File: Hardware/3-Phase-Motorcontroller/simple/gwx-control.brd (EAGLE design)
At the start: 54 x 36 mm, 25 parts, among them IC1 74LS02D, IC2 74LS123D, T1 BC850, T2 BC850

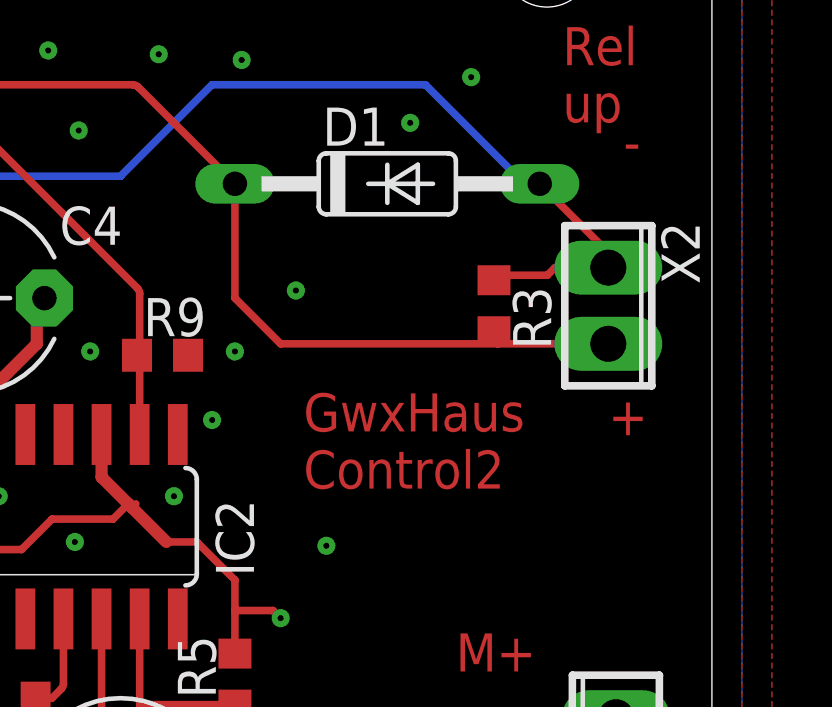
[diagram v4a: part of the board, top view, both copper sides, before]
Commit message: added alternative SMD diode
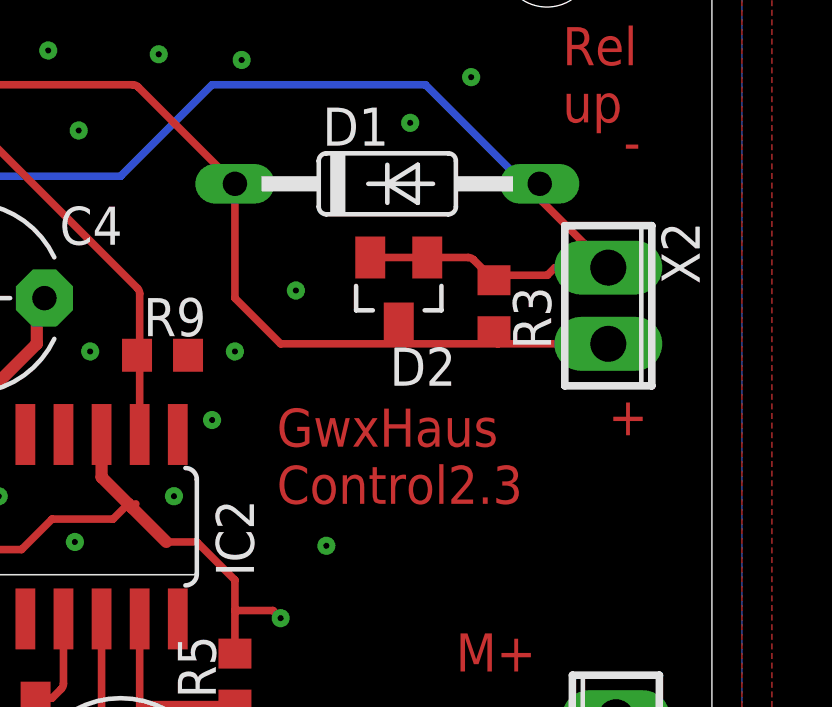
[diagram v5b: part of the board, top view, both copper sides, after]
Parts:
- added D2: BAT54C, diode:SOT23
- D1: value 1N4148DO35-10 -> 1N4148
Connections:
- net /UP: now also D2.1, D2.2
- net VCC: now also D2.3
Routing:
- net /UP: track 67.9 -> 72.3 mm
- net VCC: track 139.8 -> 140.5 mm
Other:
- board text added: "GwxHaus Control2.3"
- board text removed: "GwxHaus Control2"
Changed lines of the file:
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@@
 <text x="0.46" y="19.558" size="1.778" layer="1">eu</text>
 <text x="0.46" y="17.018" size="1.778" layer="1">ed</text>
-<text x="40.386" y="15.748" size="1.27" layer="1">GwxHaus
-Control2</text>
+<text x="39.497" y="15.24" size="1.27" layer="1">GwxHaus
+Control2.3</text>
 <text x="45.466" y="9.652" size="1.27" layer="1">M+</text>
 <text x="49.022" y="27.956" size="1.27" layer="1">Rel
@@
 </autorouter>
 <elements>
-<element name="D1" library="diode" package="DO35-10" value="1N4148DO35-10" x="43.18" y="25.908"/>
+<element name="D1" library="diode" package="DO35-10" value="1N4148" x="43.18" y="25.908"/>
 <element name="IC1" library="74xx-eu" package="SO14" value="74LS02D" x="16.51" y="14.478" smashed="yes">
 <attribute name="VALUE" x="13.335" y="13.716" size="1.27" layer="27" ratio="10"/>
@@
 <element name="T2" library="transistor" package="SOT23-BEC" value="BC850" x="27.178" y="4.953" rot="R270"/>
 <element name="R10" library="resistor" package="R0603" value="10k" x="30.607" y="8.763" rot="R180"/>
+<element name="D2" library="diode" package="SOT23" value="BAT54C" x="43.561" y="22.352" rot="R180"/>
 </elements>
 <signals>
@@
 <via x="21.844" y="21.844" extent="1-16" drill="0.2" diameter="0.254"/>
 <wire x1="38.1" y1="22.098" x2="39.624" y2="20.574" width="0.254" layer="1"/>
-<wire x1="39.624" y1="20.574" x2="46.863" y2="20.574" width="0.254" layer="1"/>
+<wire x1="39.624" y1="20.574" x2="43.688" y2="20.574" width="0.254" layer="1"/>
+<wire x1="43.688" y1="20.574" x2="46.863" y2="20.574" width="0.254" layer="1"/>
 <wire x1="46.863" y1="20.574" x2="50.546" y2="20.574" width="0.254" layer="1"/>
 <wire x1="38.1" y1="22.098" x2="38.1" y2="25.908" width="0.254" layer="1"/>
@@
 <wire x1="20.713790625" y1="7.248" x2="20.89339375" y2="7.17360625" width="0.254" layer="1" curve="-44.999502"/>
 <wire x1="20.89339375" y1="7.17360625" x2="21.1455" y2="6.9215" width="0.254" layer="1"/>
+<contactref element="D2" pad="3"/>
+<wire x1="43.561" y1="21.252" x2="43.561" y2="20.806209375" width="0.254" layer="1"/>
+<wire x1="43.561" y1="20.806209375" x2="43.63539375" y2="20.62660625" width="0.254" layer="1" curve="44.999502"/>
+<wire x1="43.63539375" y1="20.62660625" x2="43.688" y2="20.574" width="0.254" layer="1"/>
 </signal>
 <signal name="UP">
@@
 <contactref element="IC1" pad="9"/>
 <contactref element="IC1" pad="12"/>
-<contactref element="D1" pad="A"/>
 <contactref element="R3" pad="1"/>
 <contactref element="J1" pad="3"/>
@@
 <via x="15.24" y="19.304" extent="1-16" drill="0.2" diameter="0.254"/>
 <contactref element="X2" pad="1"/>
-<wire x1="48.26" y1="25.908" x2="50.546" y2="23.622" width="0.254" layer="1"/>
 <wire x1="50.546" y1="23.622" x2="50.546" y2="23.114" width="0.254" layer="1"/>
 <wire x1="21.336" y1="18.796" x2="24.384" y2="21.844" width="0.254" layer="16"/>
@@
 <wire x1="37.338" y1="29.21" x2="44.45" y2="29.21" width="0.254" layer="16"/>
 <wire x1="44.45" y1="29.21" x2="47.752" y2="25.908" width="0.254" layer="16"/>
-<wire x1="47.752" y1="25.908" x2="48.26" y2="25.908" width="0.254" layer="16"/>
 <wire x1="46.736" y1="22.694" x2="46.902" y2="22.86" width="0.254" layer="1"/>
 <wire x1="46.902" y1="22.86" x2="48.514" y2="22.86" width="0.254" layer="1"/>
@@
 <wire x1="7" y1="15" x2="5.102" y2="15" width="0.254" layer="1"/>
 <wire x1="5.102" y1="15" x2="5.08" y2="14.978" width="0.254" layer="1"/>
+<contactref element="D1" pad="A"/>
+<contactref element="D2" pad="1"/>
+<contactref element="D2" pad="2"/>
+<wire x1="42.611" y1="23.452" x2="44.511" y2="23.452" width="0.254" layer="1"/>
+<wire x1="44.511" y1="23.452" x2="45.872790625" y2="23.452" width="0.254" layer="1"/>
+<wire x1="45.872790625" y1="23.452" x2="46.05239375" y2="23.37760625" width="0.254" layer="1" curve="-44.999502"/>
+<wire x1="46.05239375" y1="23.37760625" x2="46.736" y2="22.694" width="0.254" layer="1"/>
+<wire x1="48.26" y1="25.908" x2="48.26" y2="25.505209375" width="0.254" layer="1"/>
+<wire x1="48.26" y1="25.505209375" x2="48.33439375" y2="25.32560625" width="0.254" layer="1" curve="44.999502"/>
+<wire x1="48.33439375" y1="25.32560625" x2="50.546" y2="23.114" width="0.254" layer="1"/>
+<wire x1="47.752" y1="25.908" x2="48.26" y2="25.908" width="0" layer="19" extent="16-16"/>
 </signal>
 <signal name="/END_UP">

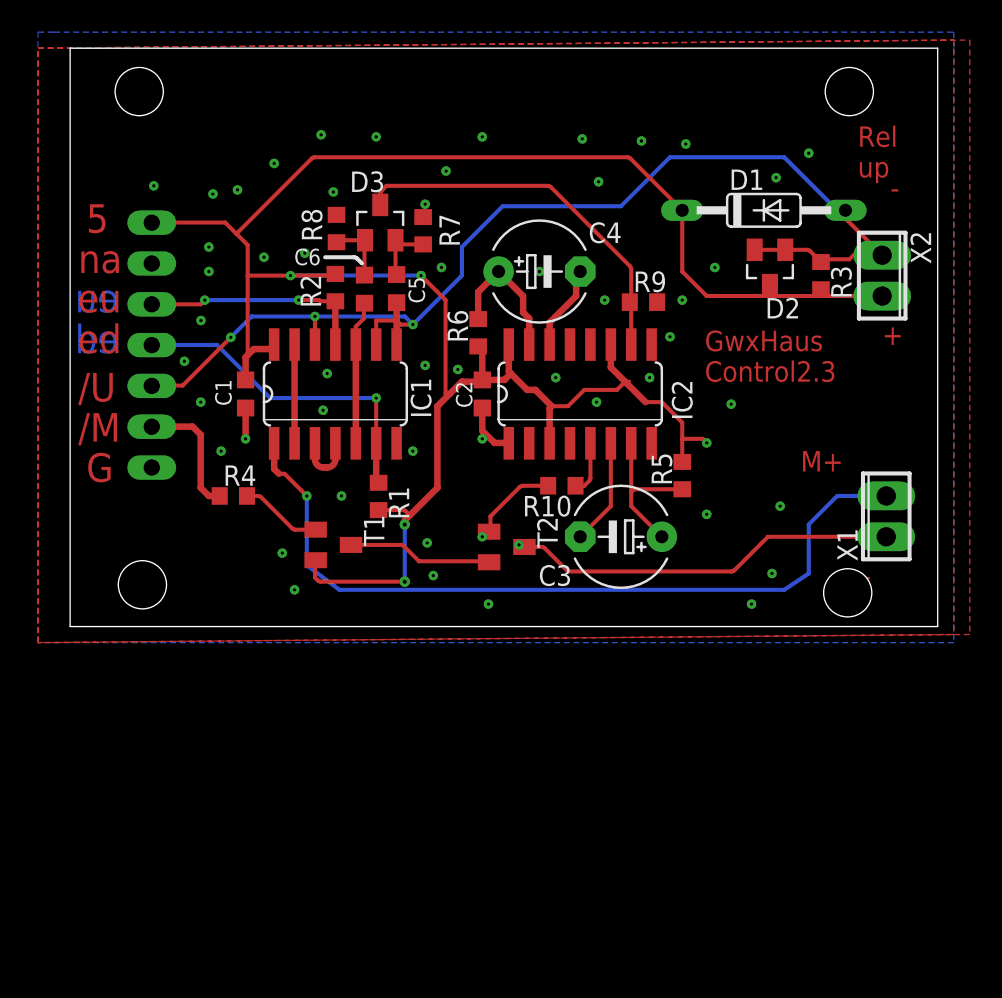
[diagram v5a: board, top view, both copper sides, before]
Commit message: pcb size cahnged to 33x54
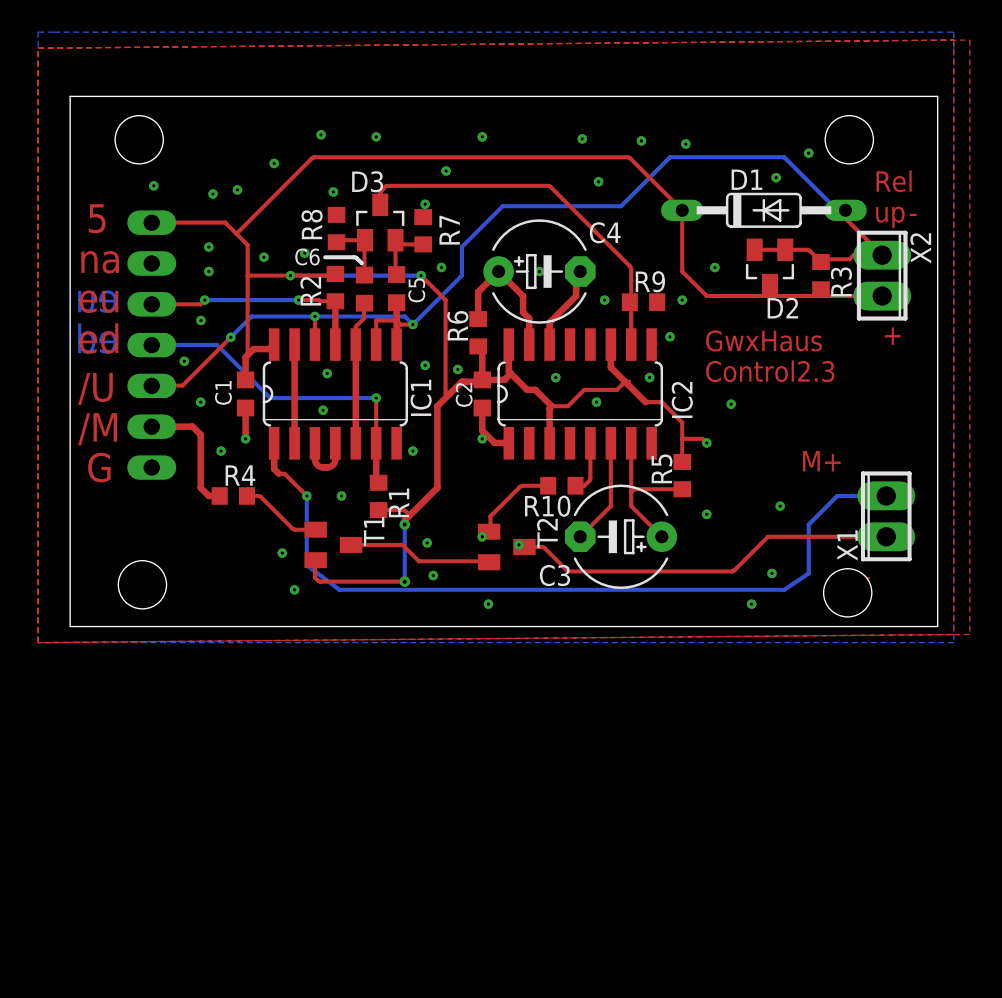
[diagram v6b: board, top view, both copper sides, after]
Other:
- board size 54 x 36 mm -> 54 x 33 mm
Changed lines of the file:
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@@
 <setting verticaltext="up"/>
 </settings>
-<grid distance="5" unitdist="mil" unit="mil" style="lines" multiple="1" display="no" altdistance="0.025" altunitdist="inch" altunit="inch"/>
+<grid distance="1" unitdist="mm" unit="mm" style="dots" multiple="1" display="no" altdistance="0.025" altunitdist="inch" altunit="inch"/>
 <layers>
 <layer number="1" name="Top" color="4" fill="1" visible="yes" active="yes"/>
@@
 <plain>
 <wire x1="0" y1="0" x2="54" y2="0" width="0" layer="20"/>
-<wire x1="54" y1="0" x2="54" y2="36" width="0" layer="20"/>
-<wire x1="54" y1="36" x2="0" y2="36" width="0" layer="20"/>
-<wire x1="0" y1="36" x2="0" y2="0" width="0" layer="20"/>
+<wire x1="54" y1="0" x2="54" y2="33" width="0" layer="20"/>
+<wire x1="54" y1="33" x2="0" y2="33" width="0" layer="20"/>
+<wire x1="0" y1="33" x2="0" y2="0" width="0" layer="20"/>
 <text x="3.04" y="19.558" size="1.778" layer="16" rot="MR0">eu</text>
 <text x="3.04" y="17.018" size="1.778" layer="16" rot="MR0">ed</text>
@@
 Control2.3</text>
 <text x="45.466" y="9.652" size="1.27" layer="1">M+</text>
-<text x="49.022" y="27.956" size="1.27" layer="1">Rel
+<text x="50.038" y="25.162" size="1.27" layer="1">Rel
 up</text>
-<text x="51.054" y="26.67" size="1.27" layer="1">-</text>
+<text x="52.197" y="25.146" size="1.27" layer="1">-</text>
 <text x="50.546" y="17.526" size="1.27" layer="1">+</text>
 <text x="49.276" y="2.54" size="1.27" layer="1">-</text>
-<hole x="4.3" y="33.3" drill="3"/>
+<hole x="4.3" y="30.3" drill="3"/>
 <hole x="4.5" y="2.6" drill="3"/>
-<hole x="48.5" y="33.3" drill="3"/>
+<hole x="48.5" y="30.3" drill="3"/>
 <hole x="48.4" y="2.1" drill="3"/>
 <wire x1="15.875" y1="22.987" x2="17.674790625" y2="22.987" width="0.254" layer="25"/>

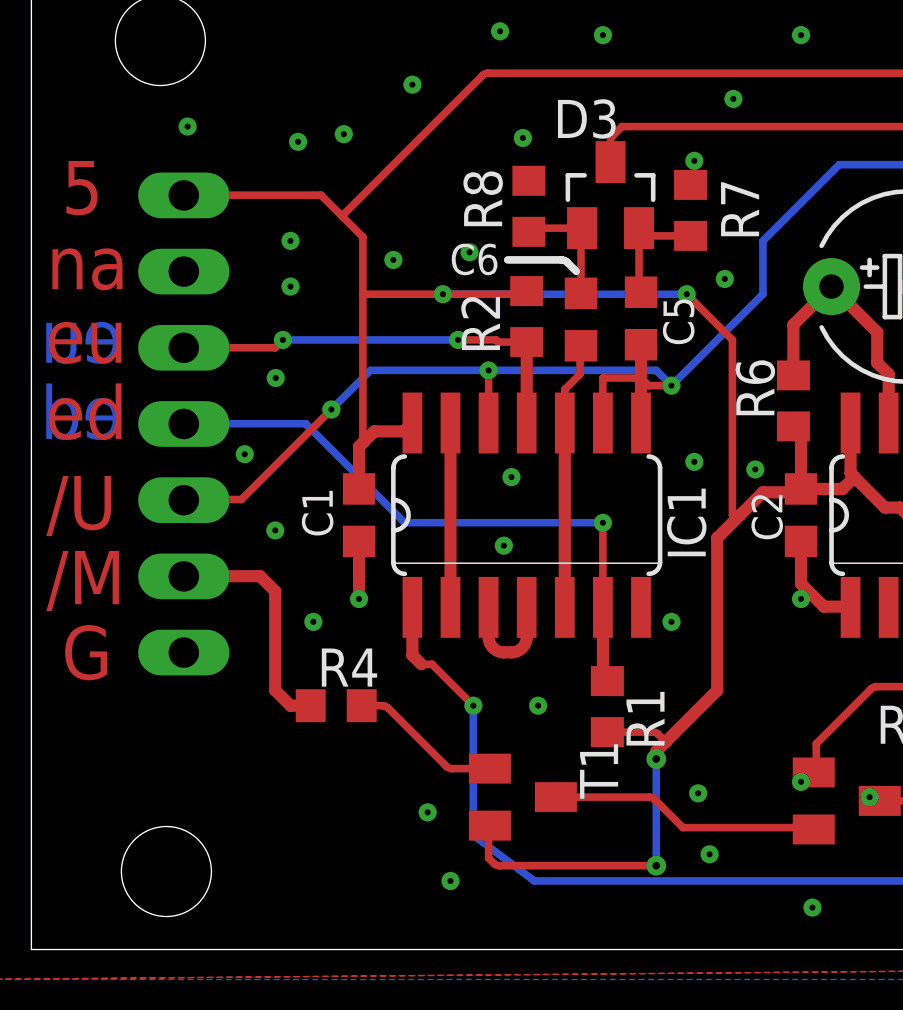
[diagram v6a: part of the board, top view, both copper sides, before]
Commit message: LEDs added
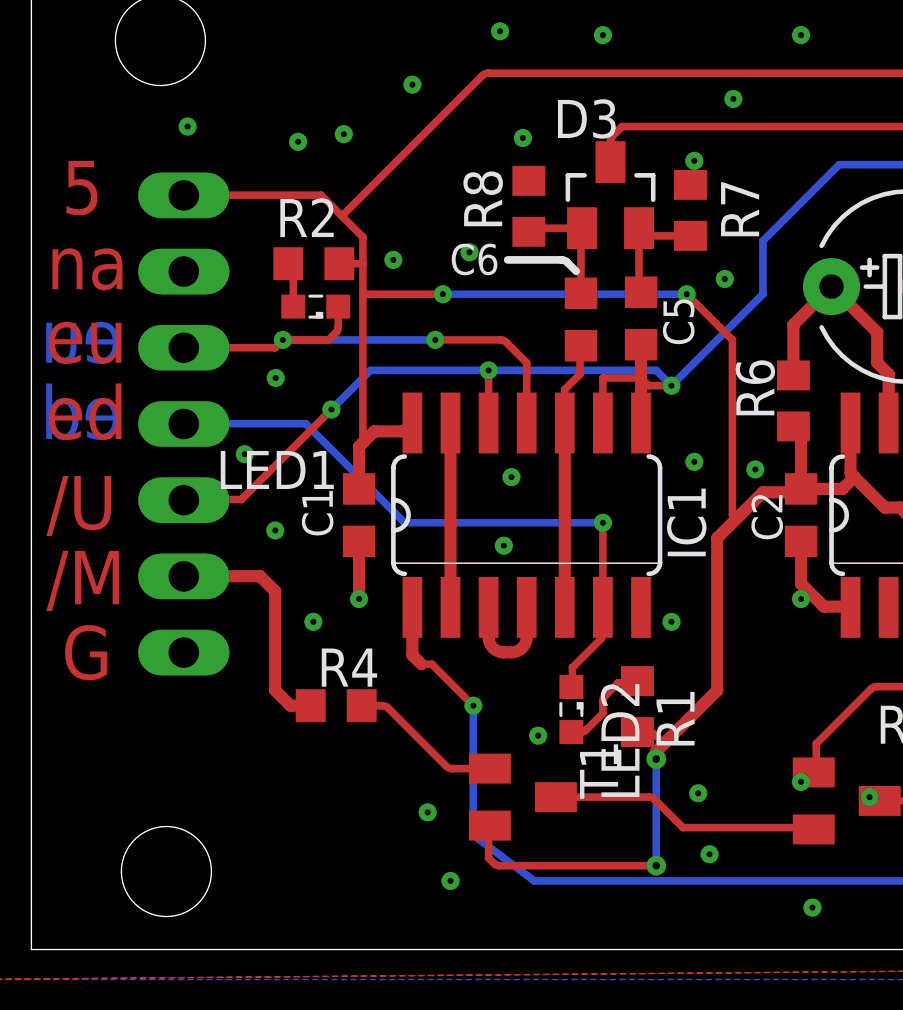
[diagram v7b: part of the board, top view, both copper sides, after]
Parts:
- added LED1, LED2: (no value), eagle-ltspice:LED_SML0603
- moved R2 7.31 mm to (9.41, 22.9), turned to 0 degrees
- moved R1 1.00 mm to (20.2, 8.10)
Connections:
- new net N$15: LED2.A, R1.1
- new net PU: LED1.A, R2.1
- net /END_DOWN: now also LED2.C; no longer R1.1
- net /END_UP: now also LED1.C; no longer R2.1
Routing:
- net N$15: track 0.00 -> 3.16 mm
- net VCC: track 140.5 -> 137.4 mm
- net /END_UP: track 14.3 -> 17.1 mm
- net PU: track 0.00 -> 1.48 mm
- net /END_DOWN: track 20.7 -> 21.2 mm
- net GND: vias 52 -> 50
